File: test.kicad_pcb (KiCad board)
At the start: 2 copper layers, 110 x 100 mm, 202 parts, among them J1 HSP2_MX-502584-0670, J2 HSP2_MX-502584-0670, J3 HSP2_MX-502584-0670, J4 HSP2_MX-502584-0670, J5 HSP2_MX-502584-0670, J6 HSP2_MX-502584-0670, J7 CONN_02X01, J8 CONN_02X01, J9 microSD, P1 Gniazdo akumulatora, P2 Gniazdo akumulatora, P3 Gniazdo programatora SWD, T1 IRLML6401, T10 BSS138, T11 BSS138, T12 BSS138, T13 BSS138, T14 FDV304P, T2 IRLML6401, T3 IRLML6401, T4 IRLML6401, T5 IRLML6401, T6 IRLML6401, T7 BSS138, T8 BSS138, T9 BSS138, U1 MCP1755T-3302E/DC, U10 TPS3823, U11 STM32L051R8, U12 DS3231SN, U13 MCP1755T-3302E/DC, U14 MCP1755T-3302E/DC, U15 MIC29302, U16 DHT22, U17 M590E, U18 S25FL1275ABMGI101, U19 ESP-07, U2 MCP1755T-3302E/DC, U20 SIMHOLDER, U3 MCP1755T-3302E/DC, U4 MCP1755T-3302E/DC, U5 MCP1755T-3302E/DC, U6 MCP1755T-3302E/DC, U7 74LVX373M, U8 74LVX373M, U9 MAX3485, Y1 32.768 kHz, Y2 8 MHz

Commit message: +nowe modele 3d. Niedokończone routowanie dth22 w innym miejscu
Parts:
- added TP16: TEST, Measurement_Points:Measurement_Point_Round-SMD-Pad_Big, F.Cu at (5.46, 135.1)
- moved TP21 75.2 mm to (29.2, 136.0)
- moved R43 73.8 mm to (36.2, 136.3), turned to 270 degrees
- moved R46 71.7 mm to (37.8, 136.3), turned to 90 degrees
- moved T14 68.1 mm to (40.5, 136.0), turned to 90 degrees
- moved R45 63.4 mm to (38.2, 131.8), turned to 180 degrees
- moved TP27 63.3 mm to (30.0, 130.8)
- moved T13 62.8 mm to (33.4, 136.0), turned to 0 degrees
- moved C41 57.1 mm to (45.3, 132.5), turned to 90 degrees
- moved C42 57.0 mm to (43.9, 132.5), turned to 90 degrees
- moved R41 28.2 mm to (100.7, 116.5)
- moved TP17 27.7 mm to (32.4, 122.8)
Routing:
- net Net-(R41-Pad1): track 1.66 -> 67.1 mm, vias 0 -> 5
- net /DHT22_ON: track 38.9 -> 2.92 mm, vias 2 -> 0
- net /DHT22_DATA: track 28.6 -> 2.53 mm, vias 2 -> 0
- net +3.3V: track 309.5 -> 299.3 mm
- net Net-(R43-Pad1): track 22.1 -> 13.1 mm
- net GND: track 1103.8 -> 1108.7 mm, vias 22 -> 24
- net +3.3VSTM: track 178.4 -> 179.4 mm
- net Net-(D2-Pad1): track 41.3 -> 40.4 mm
- net Net-(C41-Pad1): track 19.4 -> 20.0 mm

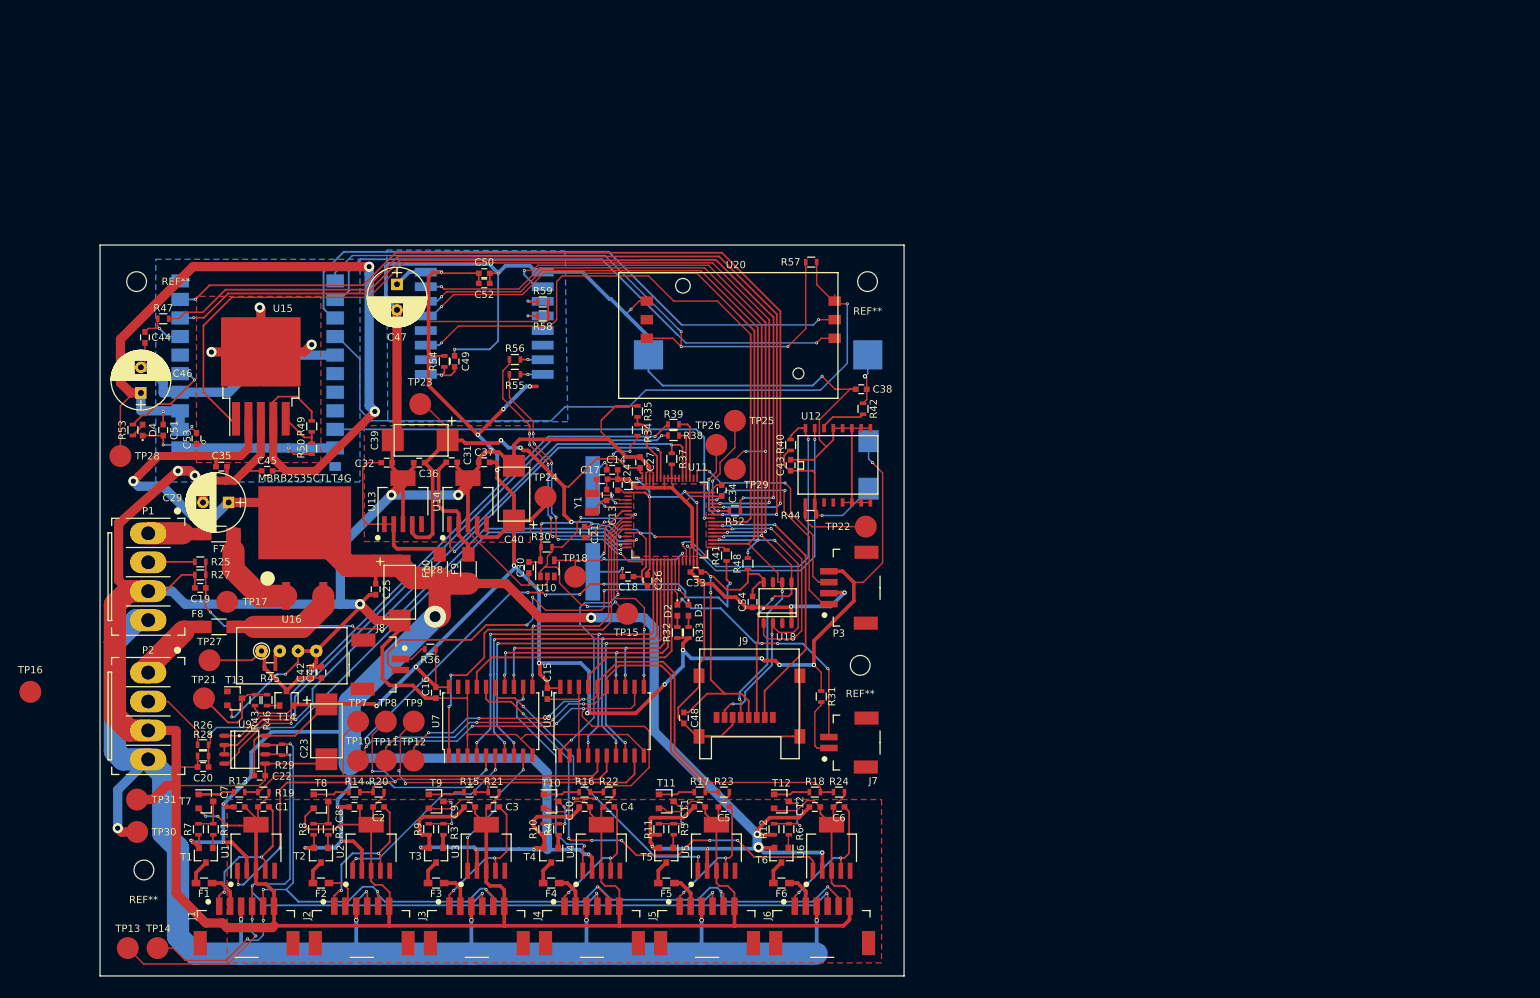
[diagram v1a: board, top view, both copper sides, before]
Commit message: routowanie dht22 w nowym miejscu
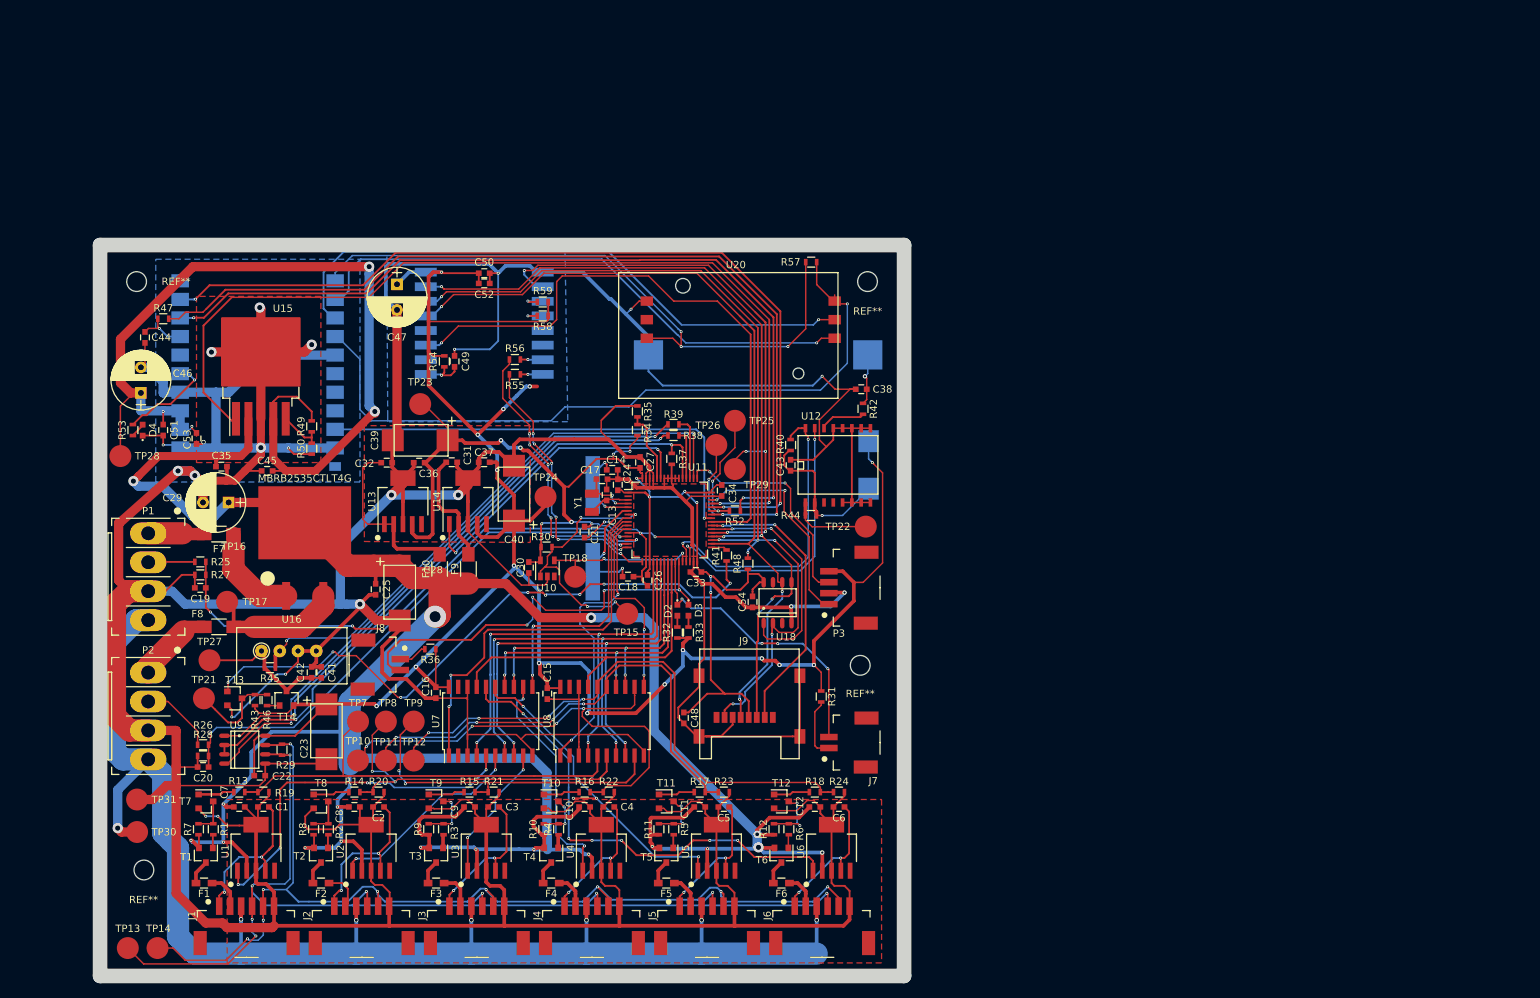
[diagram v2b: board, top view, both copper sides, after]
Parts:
- moved TP16 32.5 mm to (33.3, 118.2)
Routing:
- net /DHT22_DATA: track 2.53 -> 77.9 mm, vias 0 -> 2
- net Net-(R41-Pad1): track 67.1 -> 85.8 mm, vias 5 -> 8
- net GND: track 1108.7 -> 1125.9 mm, vias 24 -> 25
- net Net-(D1-Pad3): track 14.8 -> 18.6 mm
- net /DHT22_ON: track 2.92 -> 2.21 mm

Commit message: przesunięcie karty sim i cr2032
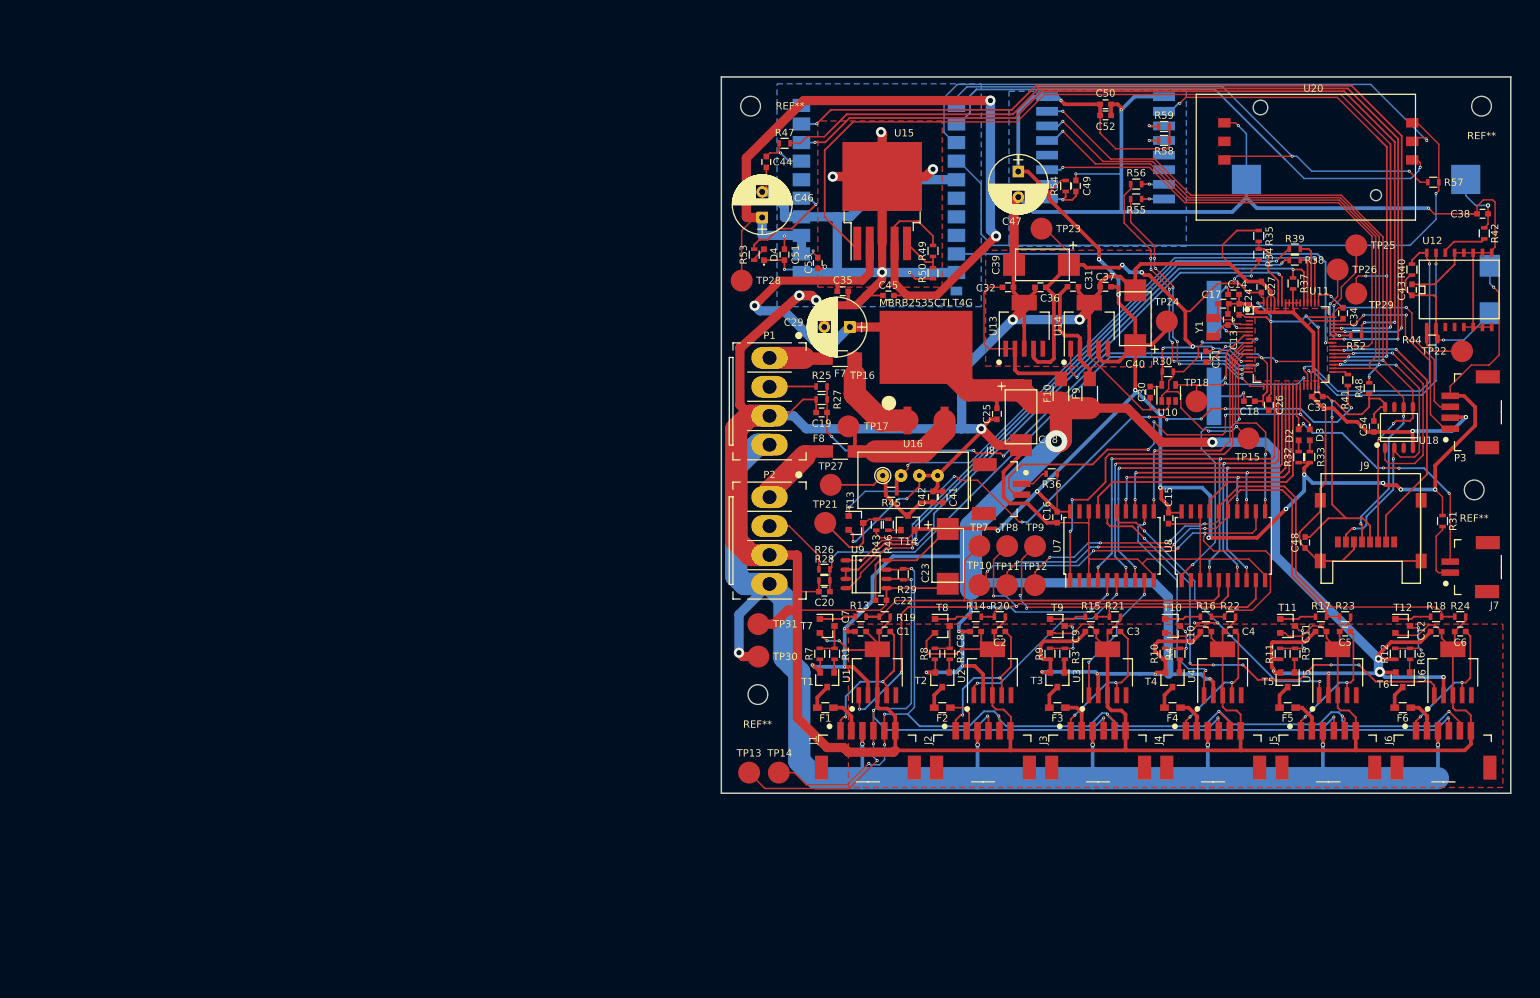
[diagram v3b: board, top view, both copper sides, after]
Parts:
- U11: footprint Housings_QFP:LQFP-64_10x10mm_Pitch0.5mm -> footprints:LQFP-64_10x10mm_Pitch0.5mm
- U18: footprint Power_Integrations:SO-8 -> footprints:SO-8
- moved C34 88.4 mm to (185.1, 83.3)
- moved U18 88.3 mm to (192.7, 99.0)
- moved C10 88.3 mm to (166.3, 126.9)
- moved C17 88.3 mm to (168.7, 82.0)
- moved C25 88.3 mm to (137.7, 97.1)
- moved C3 88.3 mm to (153.8, 126.9)
- moved C33 88.3 mm to (181.5, 94.7)
- moved C37 88.3 mm to (152.6, 79.7)
- moved C6 88.3 mm to (201.1, 126.9)
- moved F4 88.3 mm to (161.7, 137.3)
- moved J4 88.3 mm to (160.0, 147.2)
- moved J7 88.3 mm to (206.7, 118.1)
- moved P3 88.3 mm to (206.7, 96.9)
- moved R11 88.3 mm to (176.5, 129.9)
- moved R16 88.3 mm to (166.3, 124.8)
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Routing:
- net /ESP_ON: track 85.5 -> 68.7 mm
- net +3.3V: track 299.3 -> 285.6 mm, vias 16 -> 14
- net /SPI_CLK: track 113.6 -> 103.4 mm
- net /SPI_MISO: track 125.5 -> 115.8 mm
- net /SPI_MOSI: track 116.0 -> 106.6 mm
- net Net-(R57-Pad2): track 99.8 -> 91.7 mm
- net Net-(R57-Pad1): track 88.1 -> 80.9 mm, vias 3 -> 2
- net /CS_ESP: track 82.4 -> 76.6 mm
- net Net-(R44-Pad1): track 11.1 -> 7.62 mm
- net Net-(U17-Pad13): track 82.6 -> 79.3 mm
- net GND: track 1125.9 -> 1122.8 mm
- net Net-(U17-Pad12): track 77.2 -> 74.7 mm
- net /RTC_BAT: track 7.10 -> 9.09 mm
- net Net-(C45-Pad1): track 128.9 -> 127.1 mm
- net /GSM_DTR: track 124.0 -> 123.1 mm
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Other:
- board size 110 x 100 mm -> 108 x 98 mm

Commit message: cap 3d skala +2xGSM rez
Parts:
- added ?: +, footprints:+, F.Cu at (109.0, 141.0)
- added R51: 1k, Resistors_SMD:R_0603, F.Cu at (194.5, 85.8)
- added R60: 1k, Resistors_SMD:R_0603, F.Cu at (182.4, 73.8)
- moved F7 1.55 mm to (116.4, 91.1)
- moved TP16 0.93 mm to (118.4, 95.2)
- moved TP17 0.15 mm to (117.4, 99.0)
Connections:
- U17 pad 19: /GSM_ON -> Net-(R60-Pad1)
- U17 pad 9: /GSM_DTR -> Net-(R51-Pad1)
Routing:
- net Net-(R51-Pad1): track 0.00 -> 77.4 mm, vias 0 -> 1
- net /GSM_DTR: track 123.1 -> 45.6 mm, vias 3 -> 2
- net /GSM_ON: track 63.0 -> 12.0 mm
- net Net-(R60-Pad1): track 0.00 -> 51.0 mm
- net Net-(D1-Pad1): track 14.2 -> 13.0 mm
- net Net-(F7-Pad1): track 7.85 -> 8.68 mm
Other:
- board size 108 x 98 mm -> 110 x 100 mm

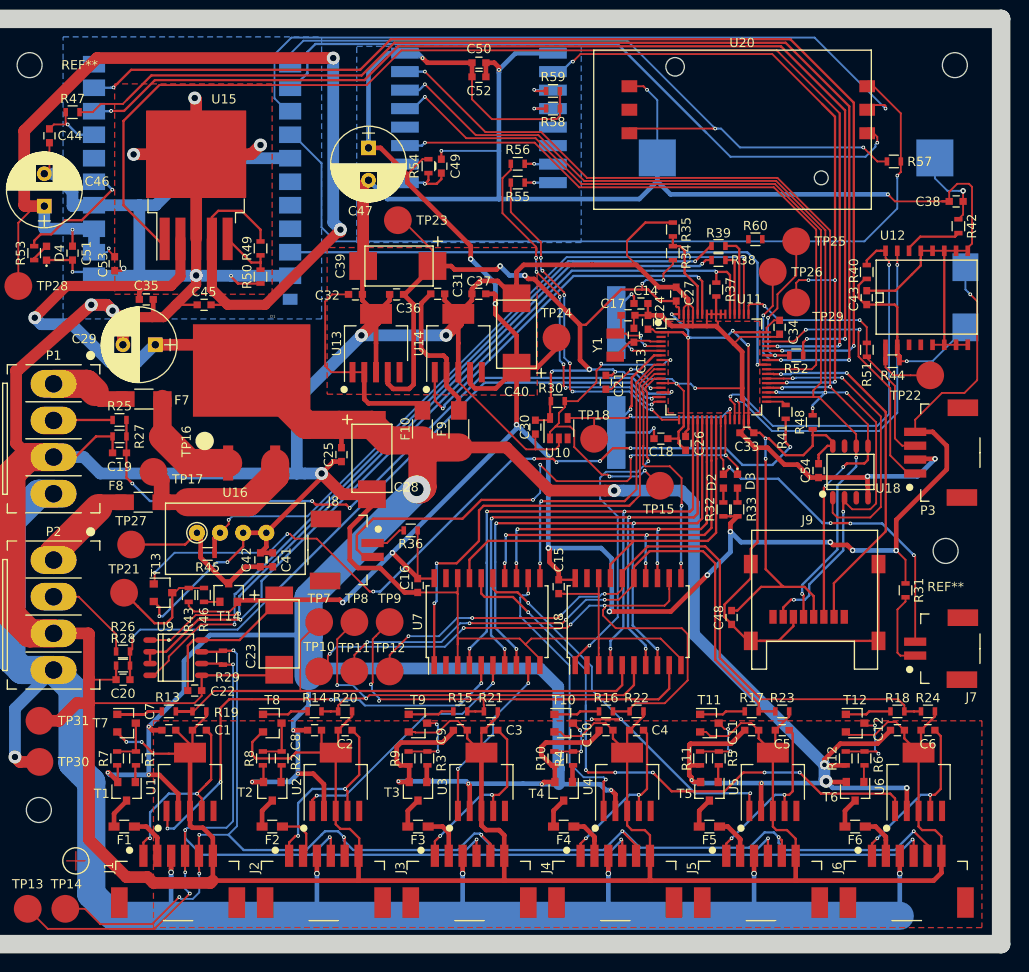
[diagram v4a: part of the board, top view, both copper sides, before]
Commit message: +tp1 tp2 zmieniono strefy miedzi
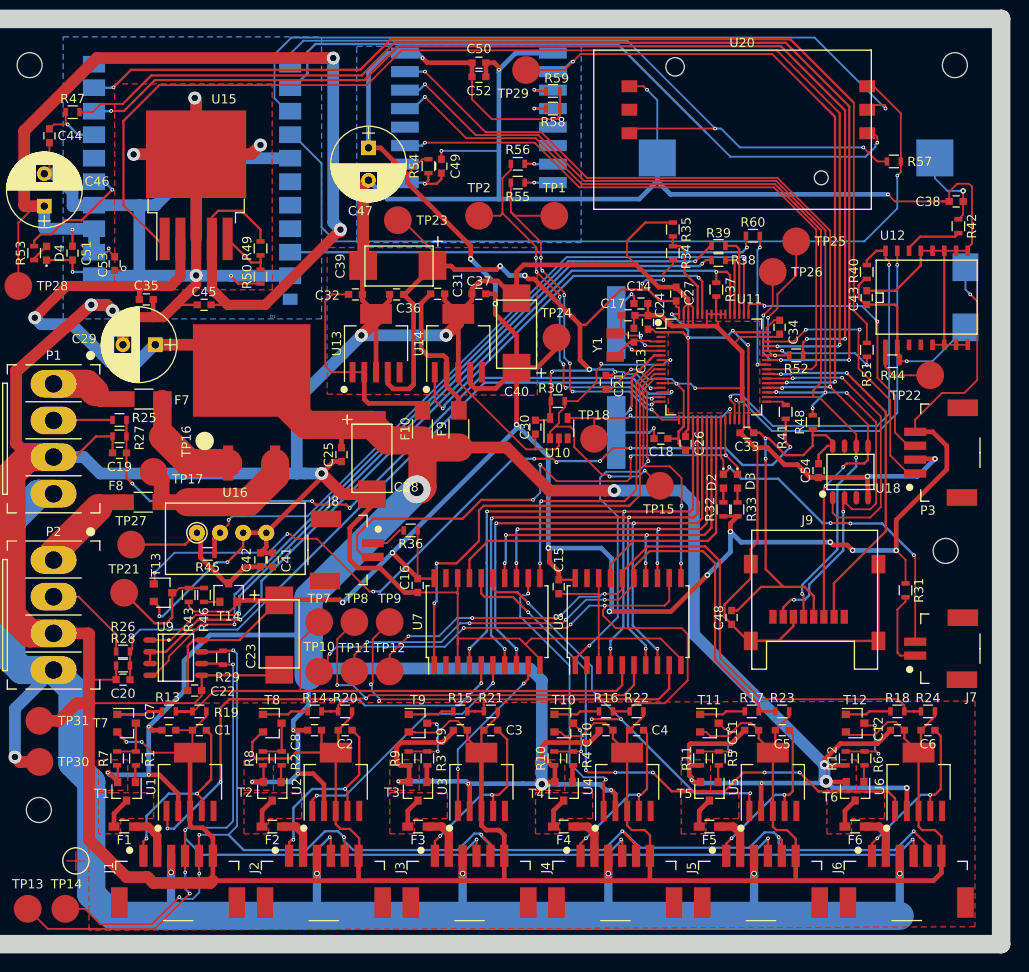
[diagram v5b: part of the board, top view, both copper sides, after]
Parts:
- added TP1: TEST, Measurement_Points:Measurement_Point_Round-SMD-Pad_Big, F.Cu at (160.7, 71.3)
- added TP2: TEST, Measurement_Points:Measurement_Point_Round-SMD-Pad_Big, F.Cu at (152.6, 71.3)
- moved TP29 38.5 mm to (157.7, 55.5)
- moved R60 0.46 mm to (182.2, 73.4)
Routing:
- net Net-(R51-Pad1): track 77.4 -> 113.7 mm
- net /GSM_DTR: track 45.6 -> 12.4 mm
- net /URT2_RX: track 38.1 -> 43.0 mm
- net /GSM_ON: track 12.0 -> 16.3 mm, vias 1 -> 2
- net GND: track 1122.8 -> 1118.7 mm
- net /URT2_TX: track 38.7 -> 41.3 mm
- net VBAT: track 399.3 -> 397.9 mm
- net /CS_ESP: track 76.6 -> 75.6 mm, vias 5 -> 3
- net Net-(P3-Pad3): track 30.6 -> 31.3 mm
- net Net-(R60-Pad1): track 51.0 -> 50.9 mm, vias 0 -> 1
- added copper zone on F.Cu, net Net-(F1-Pad2)
- added copper zone on F.Cu, net Net-(F2-Pad2)
- added copper zone on F.Cu, net Net-(F3-Pad2)
- added copper zone on F.Cu, net Net-(F4-Pad2)
- added copper zone on F.Cu, net Net-(F5-Pad2)
- added copper zone on F.Cu, net Net-(F6-Pad2)
- added copper zone on F.Cu, net VBAT

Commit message: ustalanie kosztorysu
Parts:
- removed P1, P2: Gniazdo akumulatora, footprints:MX-171813-0004
- removed P3: Gniazdo programatora SWD, footprints:MX-502584-0470
- removed U20: SIMHOLDER, footprints:AMPHENOL_SIMHOLDER_C707_10M006_049_2
- added J10: Gniazdo programatora SWD, footprints:MX-502584-0470, F.Cu at (206.7, 96.9)
- added J11: Gniazdo akumulatora, footprints:MX-171813-0004, F.Cu at (106.6, 95.4)
- added J12: Gniazdo akumulatora, footprints:MX-171813-0004, F.Cu at (106.6, 114.4)
- added J13: SIMHOLDER, footprints:AMPHENOL_SIMHOLDER_C707_10M006_049_2, F.Cu at (189.6, 66.7)
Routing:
- net /CS_ESP: track 75.6 -> 70.5 mm
- net /GSM_STAB_EN: track 132.7 -> 136.3 mm
- net Net-(R53-Pad1): track 13.7 -> 12.0 mm

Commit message: routowanie nowego esp
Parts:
- removed C49: 100n, Capacitors_SMD:C_0603
- removed TP23: TEST, Measurement_Points:Measurement_Point_Round-SMD-Pad_Big
- added J14: BTN1, footprints:MX-502584-0270, F.Cu at (185.9, 104.6)
- added J15: BTN2, footprints:MX-502584-0270, F.Cu at (148.4, 102.6)
- added R61: 1k, Resistors_SMD:R_0603, F.Cu at (154.2, 74.3)
- added R62: 1k, Resistors_SMD:R_0603, F.Cu at (152.7, 74.3)
- added R63: 1k, Resistors_SMD:R_0603, F.Cu at (146.7, 73.1)
- added R64: 1k, Resistors_SMD:R_0603, F.Cu at (145.2, 73.1)
- added R65: 1k, Resistors_SMD:R_0603, F.Cu at (143.7, 73.0)
- R54, R58, R59: value 10k -> 1k
- U19: value ESP-07 -> ESP-WROOM-32; footprint footprints:ESP-07 -> footprints:ESP-WROOM-32
- moved U19 29.2 mm to (160.2, 76.9), turned to 180 degrees
- moved TP1 24.8 mm to (162.0, 46.5)
- moved TP2 24.5 mm to (153.1, 46.8)
- moved R54 18.6 mm to (164.1, 73.3), turned to 90 degrees
- moved R58 17.4 mm to (163.9, 76.7), turned to 0 degrees
- moved R59 17.2 mm to (155.8, 74.3), turned to 90 degrees
- moved R55 11.8 mm to (146.1, 62.6), turned to 0 degrees
- moved R56 10.7 mm to (146.1, 64.3), turned to 0 degrees
- moved C52 9.68 mm to (161.7, 59.5), turned to 90 degrees
- moved TP29 9.02 mm to (157.8, 46.5)
- moved C50 8.96 mm to (160.2, 59.5), turned to 90 degrees
- moved R35 2.98 mm to (172.0, 75.3), turned to 90 degrees
- moved C47 1.26 mm to (139.4, 64.0)
- moved TP24 0.95 mm to (161.2, 85.4)
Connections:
- R54 pad 1: +3.3V -> Net-(R54-Pad1)
- R54 pad 2: Net-(C49-Pad1) -> /SPI_CLK
- R58 pad 1: +3.3V -> Net-(R58-Pad1)
- R58 pad 2: Net-(R58-Pad2) -> /SPI_MISO
- R59 pad 1: +3.3V -> Net-(R59-Pad1)
- R59 pad 2: Net-(R59-Pad2) -> /SPI_MOSI
- U11 pad 54: GND -> /ESP_IO0
- U11 pad 55: GND -> /ESP_IO2
- U11 pad 56: GND -> /BTN2
- U11 pad 57: GND -> /BTN1
- U11 pad 58: GND -> Net-(U11-Pad58)
- U19 pad 1: Net-(C49-Pad1) -> GND
- U19 pad 10: /CS_ESP -> Net-(U19-Pad10)
- U19 pad 11: Net-(R59-Pad2) -> Net-(U19-Pad11)
- U19 pad 12: Net-(R58-Pad2) -> Net-(U19-Pad12)
- U19 pad 13: Net-(U19-Pad13) -> Net-(R54-Pad1)
- U19 pad 14: Net-(U19-Pad14) -> Net-(R58-Pad1)
- U19 pad 15: Net-(R56-Pad1) -> GND
- U19 pad 16: Net-(R55-Pad1) -> Net-(R59-Pad1)
- U19 pad 2: Net-(U19-Pad2) -> +3.3V
- U19 pad 5: /SPI_CLK -> Net-(U19-Pad5)
- U19 pad 6: /SPI_MISO -> Net-(U19-Pad6)
- U19 pad 7: /SPI_MOSI -> Net-(U19-Pad7)
- U19 pad 8: +3.3V -> Net-(U19-Pad8)
- U19 pad 9: GND -> Net-(U19-Pad9)
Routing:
- net GND: track 1118.9 -> 1069.6 mm
- net /GSM_STAB_EN: track 136.3 -> 94.3 mm
- net /URT2_TX: track 41.3 -> 13.9 mm, vias 6 -> 3
- net /URT2_RX: track 43.0 -> 15.9 mm, vias 6 -> 3
- net /ESP_IO0: track 0.00 -> 14.2 mm
- net /ESP_IO2: track 0.00 -> 12.5 mm
- net /SPI_MOSI: track 106.6 -> 95.2 mm, vias 5 -> 4
- net /CS_ESP: track 70.5 -> 59.2 mm, vias 3 -> 2
- net /SPI_MISO: track 115.7 -> 105.5 mm, vias 7 -> 6
- net /SPI_CLK: track 103.3 -> 94.3 mm, vias 3 -> 2
- net Net-(J13-Pad1): track 91.7 -> 99.8 mm
- net +3.3VSTM: track 179.6 -> 172.2 mm, vias 14 -> 12
- net Net-(C49-Pad1): track 6.16 -> 0.00 mm, vias 1 -> 0
- net +3.3V: track 285.6 -> 280.0 mm
- net Net-(R60-Pad1): track 50.9 -> 56.5 mm
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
